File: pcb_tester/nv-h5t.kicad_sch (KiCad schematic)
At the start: 16 parts, among them J1 PSH02-03, U1 ATtiny25-20SS

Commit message: NV-H5B tester -> NV-H5T.
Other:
- company: S-COM decoder with LEDs -> S-COM testing decoder with LEDs directly on PCB
- title: NV-H5B test signal -> NV-H5T
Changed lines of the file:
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@@
   (paper "A5")
   (title_block
-    (title "NV-H5B test signal")
+    (title "NV-H5T")
     (date "2023-03-09")
     (rev "1.0")
-    (company "S-COM decoder with LEDs")
+    (company "S-COM testing decoder with LEDs directly on PCB")
     (comment 1 "Model Railroader Club Brno I – KMŽ Brno I – https://kmz-brno.cz/")
     (comment 2 "Jan Horáček")

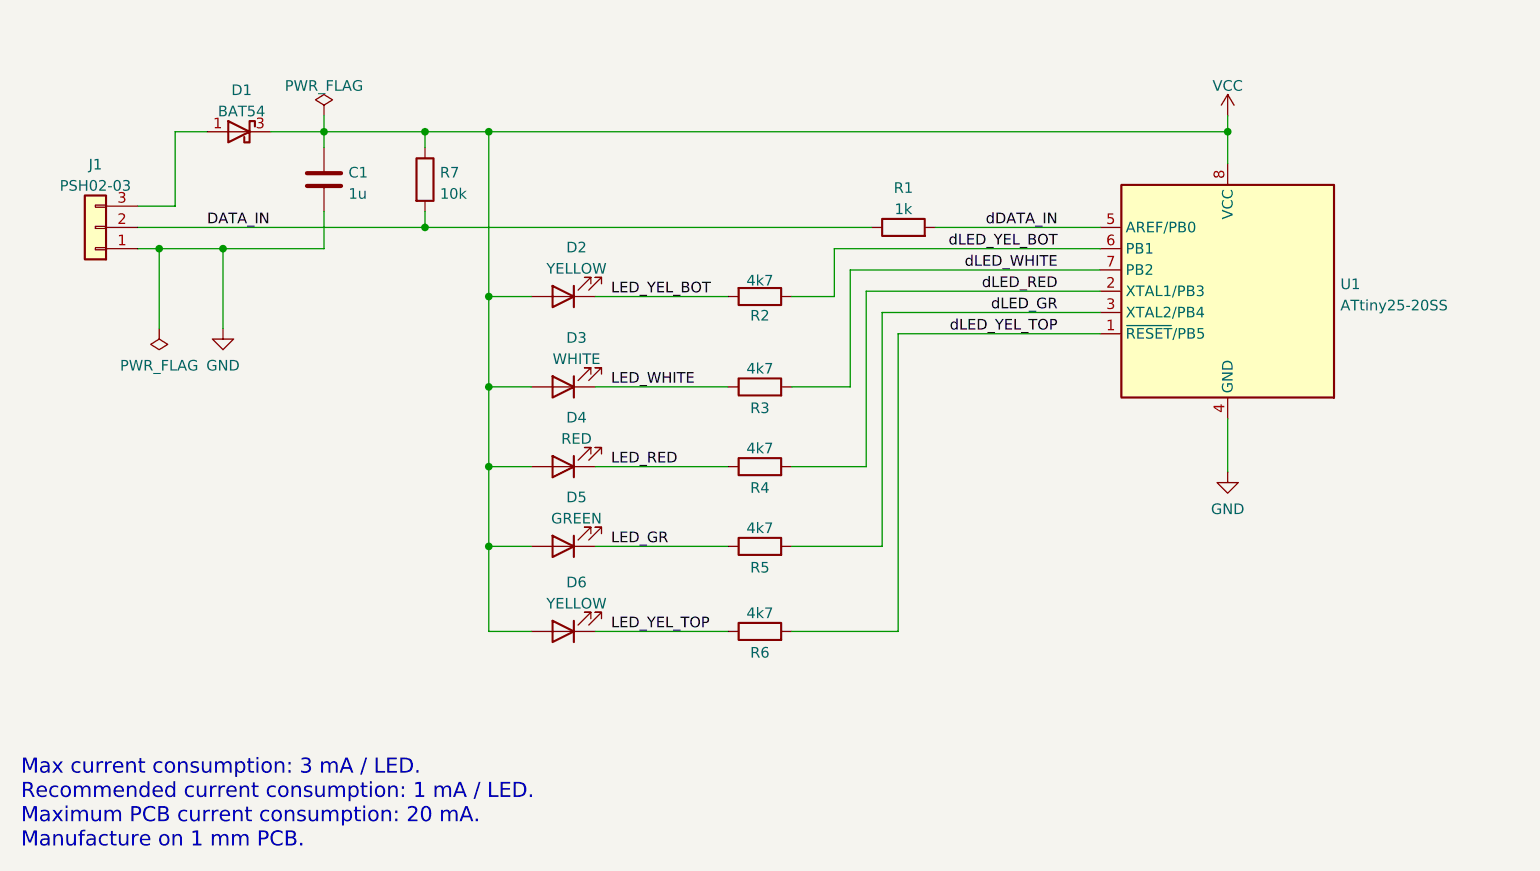
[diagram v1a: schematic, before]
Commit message: Add 3V3 stabilizer, so NV-H5T supports both 5V & 12V power supply.
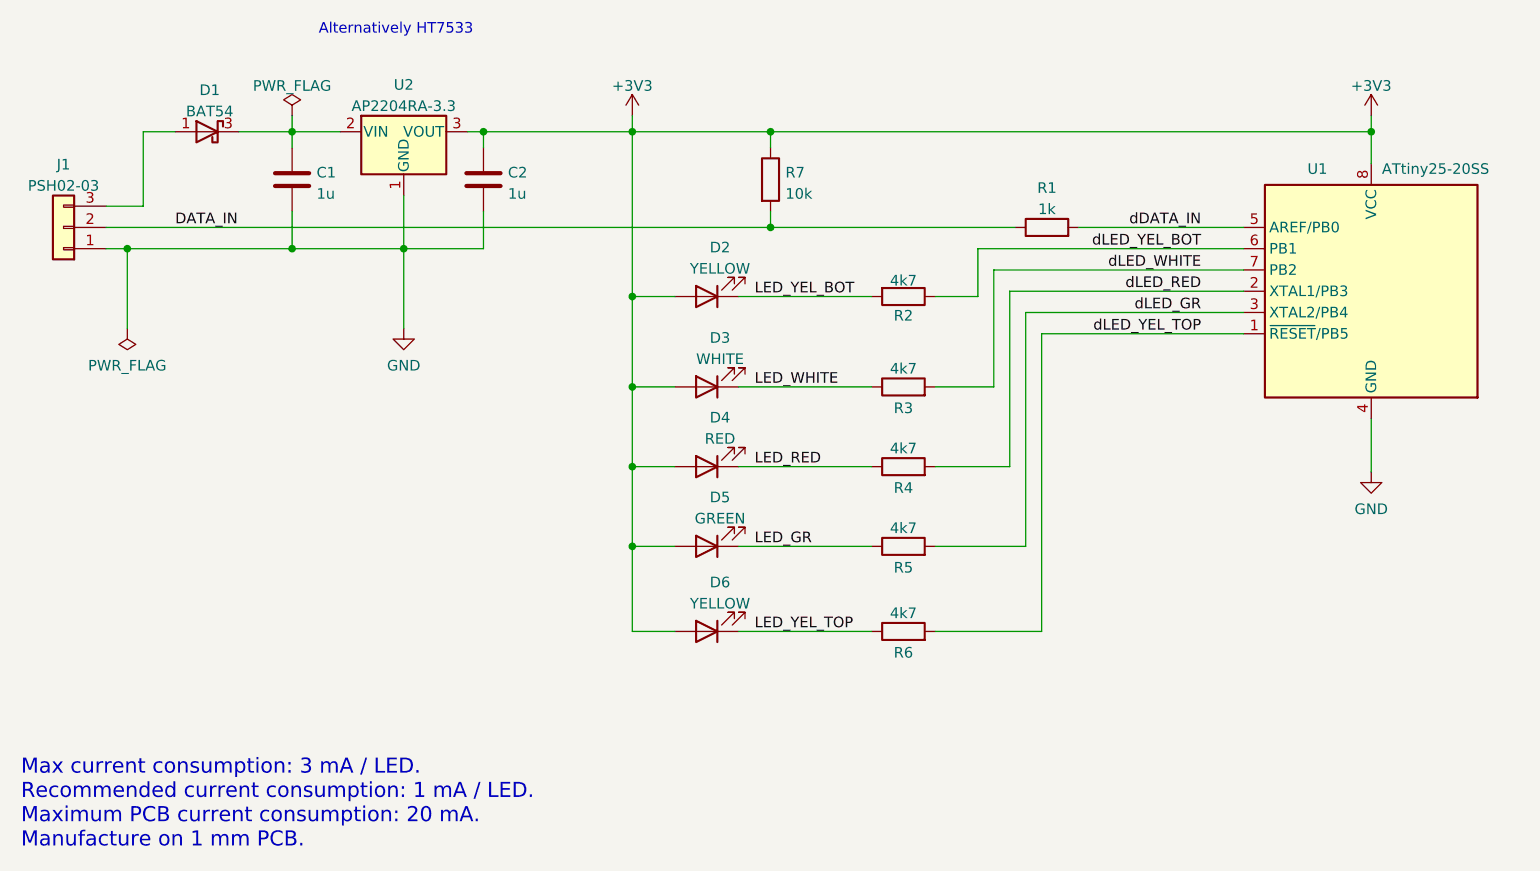
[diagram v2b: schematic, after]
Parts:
- added C2: 1u, Capacitor_SMD:C_0805_2012Metric, symbol Device:C
- added U2: AP2204RA-3.3, Package_TO_SOT_SMD:SOT-89-3, symbol Regulator_Linear:AP2204RA-3.3
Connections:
- net GND: now also C2.2, U2.1 (GND)
- net VCC renamed +3V3
- net +3V3: now also C2.1, U2.3 (VOUT); no longer C1.1, D1.3 (K)
- new net: C1.1, D1.3 (K), U2.2 (VIN)
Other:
- note added: "Alternatively HT7533"
- moved on the sheet: C1, D1, D2, D3, D4, D5, D6, J1, R1, R2, R3, R4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

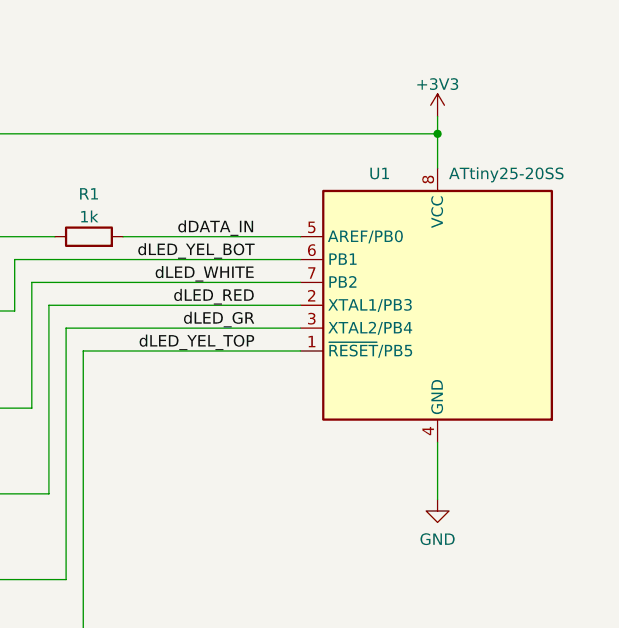
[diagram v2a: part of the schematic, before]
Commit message: Note possible alterantive versions of MCU.
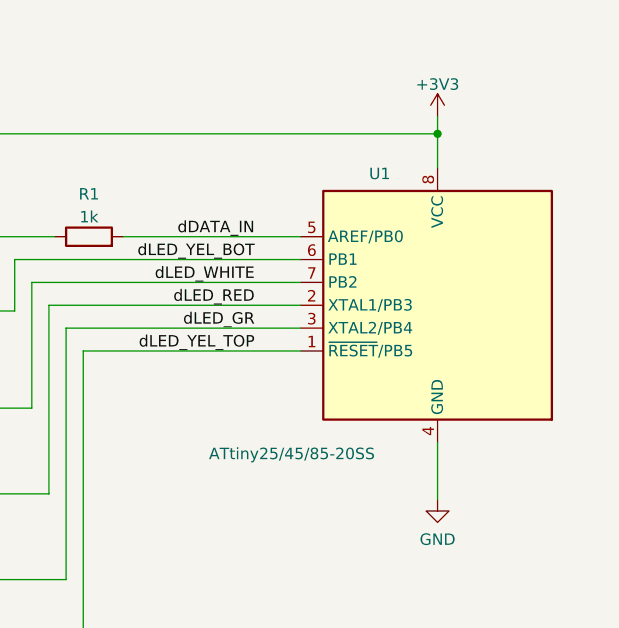
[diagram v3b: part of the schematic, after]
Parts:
- U1: value ATtiny25-20SS -> ATtiny25/45/85-20SS
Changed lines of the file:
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@@
       (effects (font (size 1.27 1.27)) (justify right))
     )
-    (property "Value" "ATtiny25-20SS" (id 1) (at 179.705 42.545 0)
+    (property "Value" "ATtiny25/45/85-20SS" (id 1) (at 153.035 73.66 0)
       (effects (font (size 1.27 1.27)) (justify right))
     )
@@
     )
     (path "/649f065c-fb95-4c73-a5ab-be6944c60862"
-      (reference "U1") (unit 1) (value "ATtiny25-20SS") (footprint "Package_SO:SOIC-8_3.9x4.9mm_P1.27mm")
+      (reference "U1") (unit 1) (value "ATtiny25/45/85-20SS") (footprint "Package_SO:SOIC-8_3.9x4.9mm_P1.27mm")
     )
     (path "/18a4bb6d-9d79-44c8-afff-840695e08fa2"
